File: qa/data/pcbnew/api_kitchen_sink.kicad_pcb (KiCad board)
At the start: 2 copper layers, 223.1 x 141.3 mm, 3 parts, among them P2 CONN_2

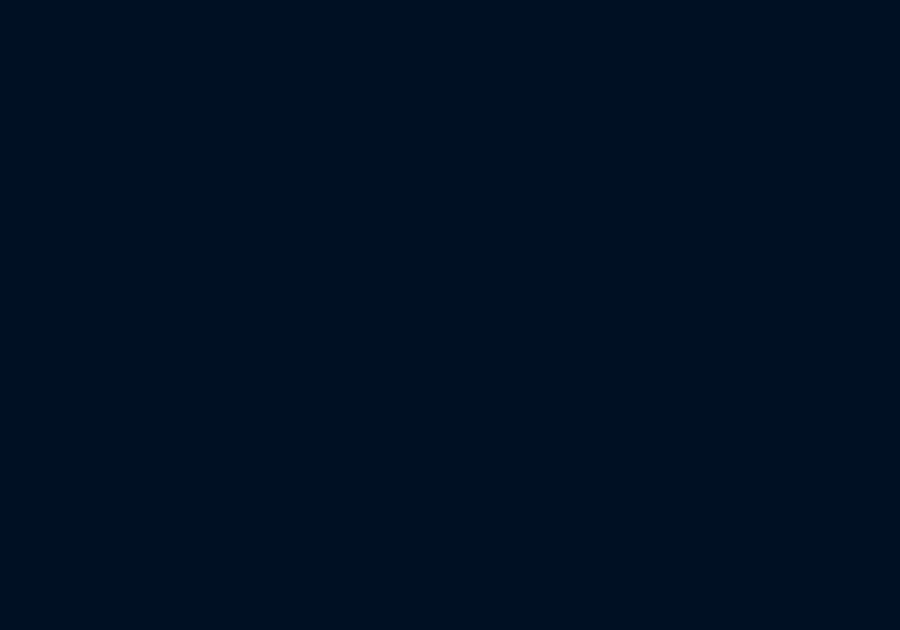
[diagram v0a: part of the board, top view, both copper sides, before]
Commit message: Release 1.3.0
Manufacturer integration and symbol/footprint generation

## New Features
  - Symbol and footprint generation for AI-assisted design
  - Diagnostic logging
  - Manufacturer integration
  - Route trace functionality

Co-authored-by: Cursor <cursoragent@cursor.com>
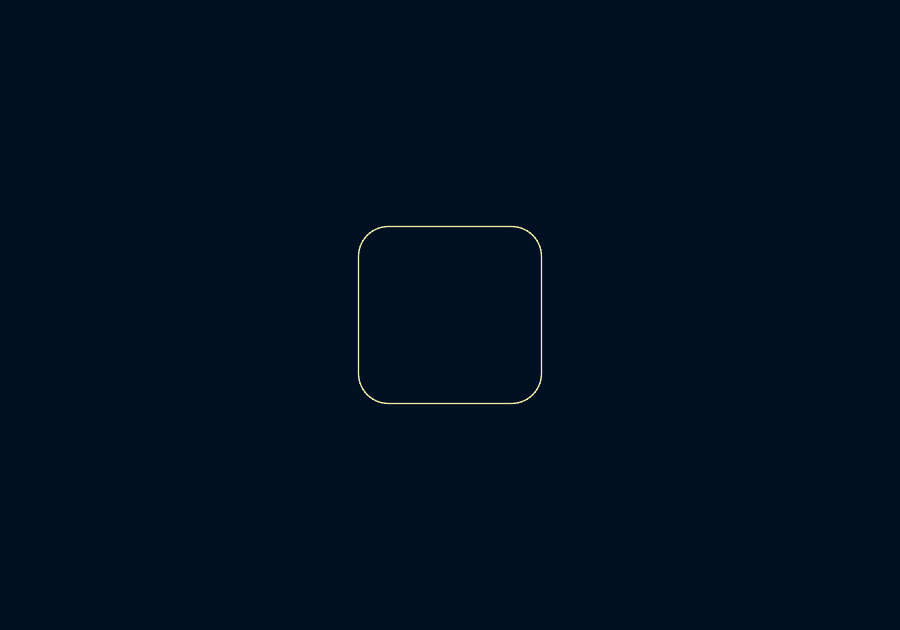
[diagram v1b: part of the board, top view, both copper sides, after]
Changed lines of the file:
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@@
+			)
+		)
+		(property "CustomField" "CustomValue"
+			(at 0 0 0)
+			(unlocked yes)
+			(layer "F.Fab")
+			(hide yes)
+			(effects
+				(font
+					(size 1 1)
+					(thickness 0.15)
+				)
 			)
 		)
@@
 		)
 	)
+	(gr_poly
+		(pts
+			(arc
+				(start 85.1 125.9)
+				(mid 85.807107 125.607107)
+				(end 86.1 124.9)
+			)
+			(arc
+				(start 86.1 121)
+				(mid 85.807107 120.292893)
+				(end 85.1 120)
+			)
+			(arc
+				(start 81 120)
+				(mid 80.292893 120.292893)
+				(end 80 121)
+			)
+			(arc
+				(start 80 124.9)
+				(mid 80.292893 125.607107)
+				(end 81 125.9)
+			)
+		)
+		(stroke
+			(width 0)
+			(type solid)
+		)
+		(fill no)
+		(layer "F.SilkS")
+	)
 	(gr_arc
 		(start 111.5 55)
@@
 	)
 	(gr_circle
+		(center 197.75 63.3)
+		(end 199.05 65.4)
+		(stroke
+			(width 0.05)
+			(type default)
+		)
+		(fill no)
+		(layer "Edge.Cuts")
+	)
+	(gr_circle
 		(center 224.6 97.7)
 		(end 228.25 99.55)
-		(stroke
-			(width 0.05)
-			(type default)
-		)
-		(fill no)
-		(layer "Edge.Cuts")
-	)
-	(gr_circle
-		(center 197.75 63.3)
-		(end 199.05 65.4)
 		(stroke
 			(width 0.05)
@@
 		)
 		(fill no)
+		(layer "B.Fab")
+	)
+	(gr_rect
+		(start 95 51)
+		(end 100 52)
+		(stroke
+			(width 0)
+			(type solid)
+		)
+		(fill yes)
 		(layer "B.Fab")
 	)
@@
 		(layer "B.Fab")
 	)
-	(gr_rect
-		(start 95 51)
-		(end 100 52)
-		(stroke
-			(width 0)
-			(type solid)
-		)
-		(fill yes)
-		(layer "B.Fab")
+	(gr_line
+		(start 111 46.5)
+		(end 115.5 54)
+		(stroke
+			(width 0.1)
+			(type default)
+		)
+		(layer "User.4")
 	)
 	(gr_line
@@
 		(stroke
 			(width 0.1)
-			(type default)
-		)
-		(layer "User.4")
-	)
-	(gr_line
-		(start 111 46.5)
-		(end 115.5 54)
-		(stroke
-			(width 0.1)
